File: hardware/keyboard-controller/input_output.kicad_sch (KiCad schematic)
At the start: 20 parts, among them J4 SYNC_IN, J5 CV_OUT, J6 GATE_OUT, J7 SYNC_OUT, Q1 2N3904, U9 LM358

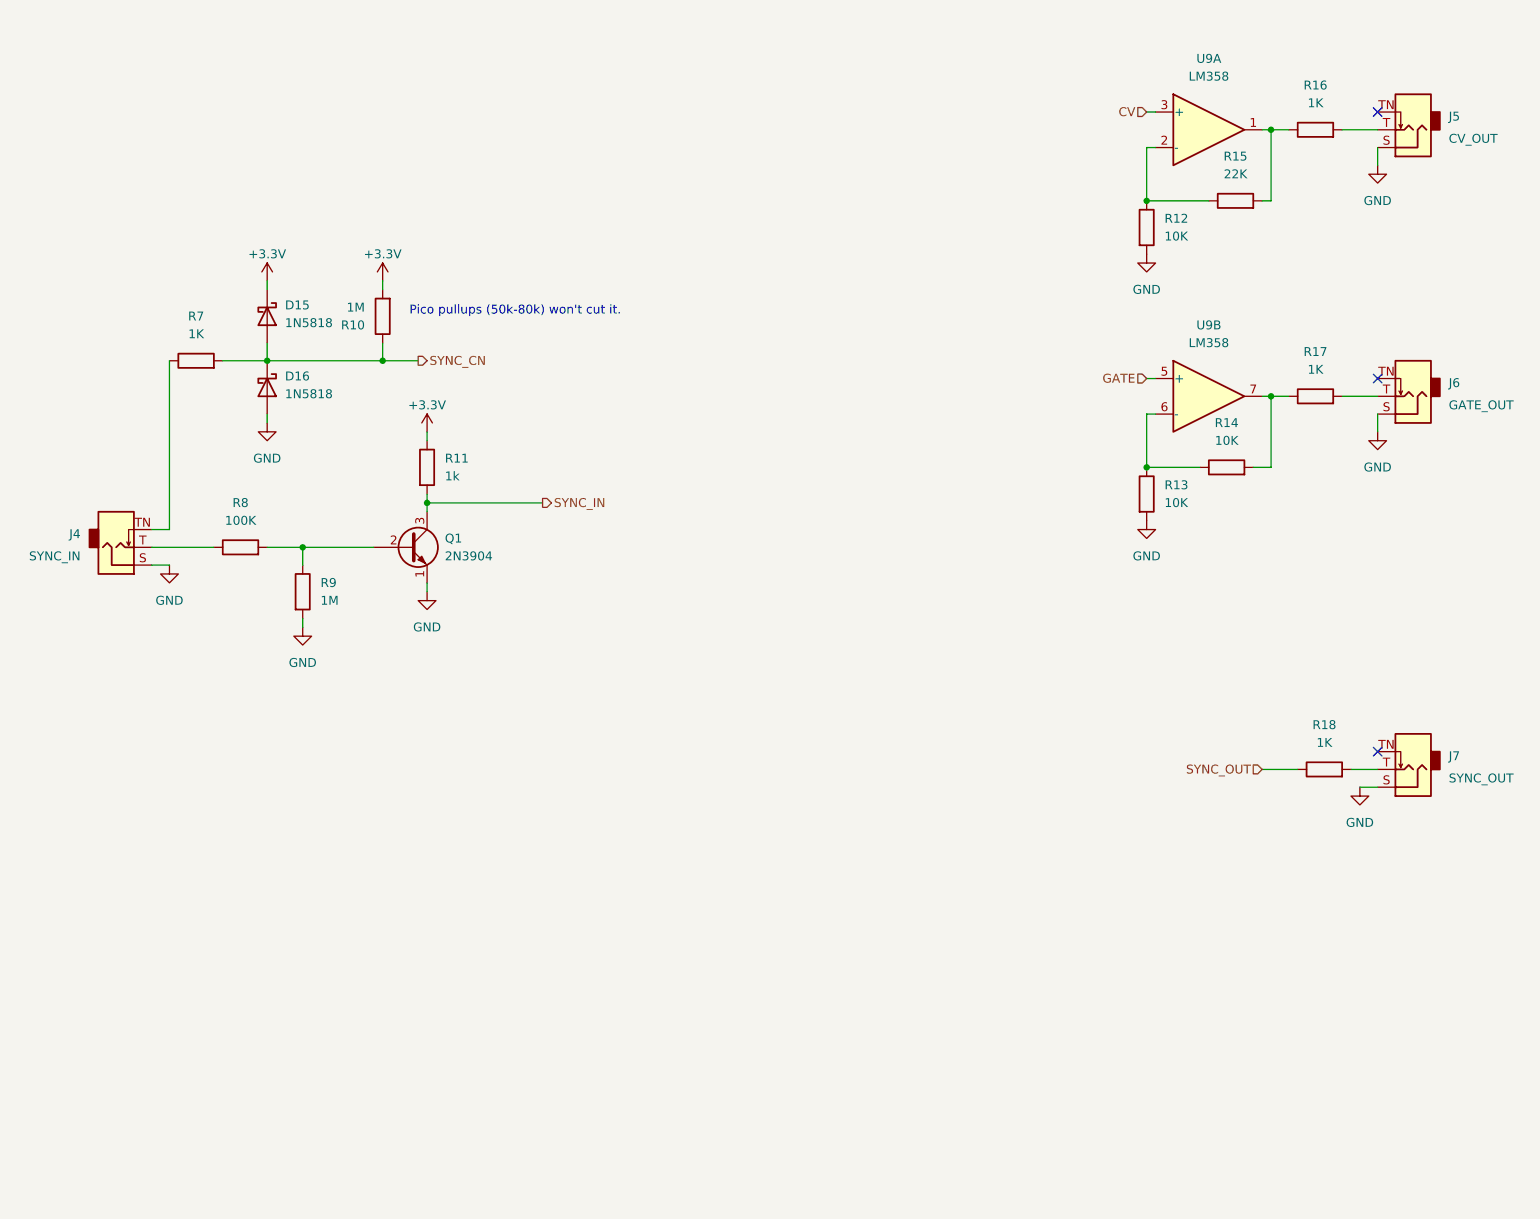
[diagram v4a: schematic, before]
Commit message: Completed schematic rev1. Started placing pcb
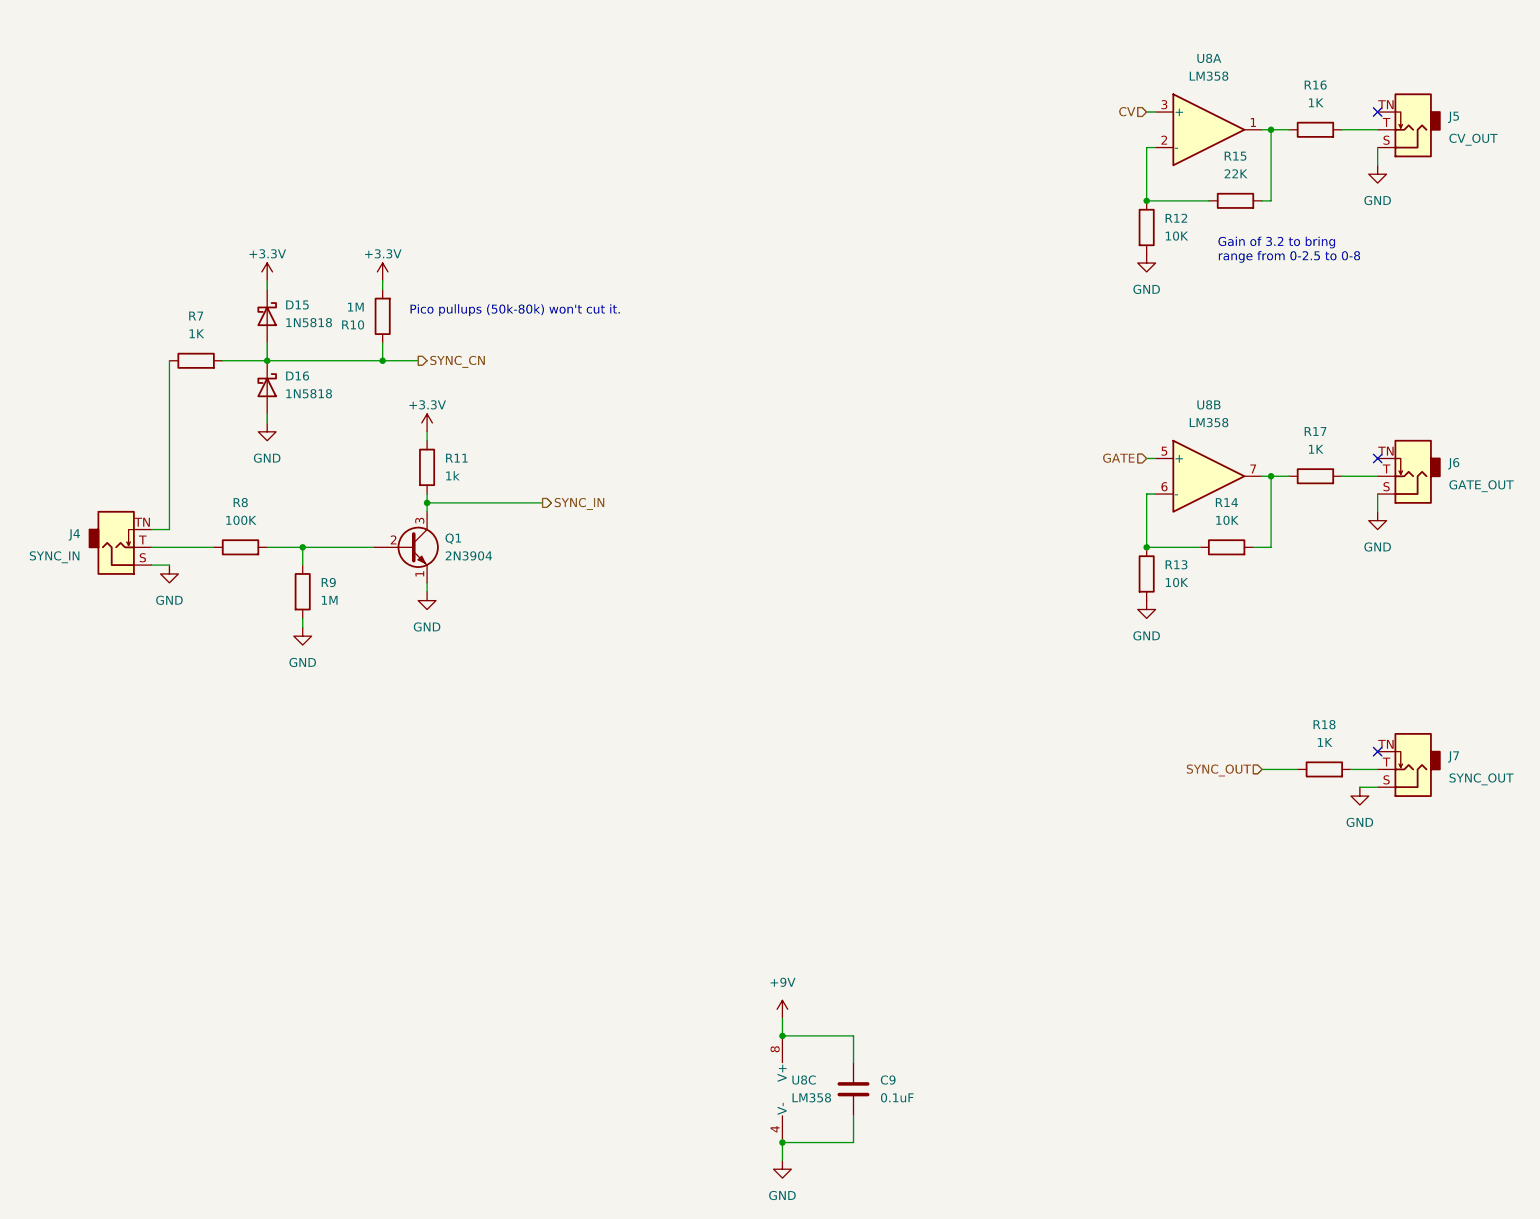
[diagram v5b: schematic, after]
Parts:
- added C9: 0.1uF, AEC_Capacitors:C_Disc_D5.0mm_W2.5mm_P3.0mm, symbol Device:C
- added unit 3 of U8
- R10, R11, R18, R7, R8, R9: footprint (none) -> Royal_Ohm_Resistors:R_Axial_DIN0207_L6.8mm_D2.5mm_P10.16mm_Horizontal
- renumbered U9 to U8
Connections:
- net GND: now also C9.2, U8.4 (V-)
- new net +9V: C9.1, U8.8 (V+)
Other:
- note added: "Gain of 3.2 to bring range from 0-2.5 to 0-8"
- moved on the sheet: J6, R13, R14, R17, U8B

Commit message: Completed initial pcb design
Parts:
- added C9: 0.1uF, AEC_Capacitors:C_Disc_D5.0mm_W2.5mm_P3.0mm, symbol Device:C
- added R14: 20K, Royal_Ohm_Resistors:R_Axial_DIN0207_L6.8mm_D2.5mm_P10.16mm_Horizontal, symbol Device:R
- added R17: 10K, Royal_Ohm_Resistors:R_Axial_DIN0207_L6.8mm_D2.5mm_P10.16mm_Horizontal, symbol Device:R
- added U8: LM358, Package_DIP:DIP-8_W7.62mm_Socket, symbol Amplifier_Operational:LM358
- R13: value 10K -> 20K
- renumbered C9 to C10, R14 to R15, R15 to R16, R16 to R18, R17 to R19, R18 to R20, U8 to U9
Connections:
- net +9V: now also C9.1, U8.8 (V+)
- net GND: now also C9.2, R14.2, U8.4 (V-), U8.5 (+)
- net SYNC_OUT: now also U8.3 (+); no longer R20.1
- net +3V3 renamed +3.3V
- new net: R14.1, R17.1, U8.2 (-)
- new net: U8.6 (-), U8.7
- new net: R17.2, R20.1, U8.1
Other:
- note added: "3.3v pulse -> 5v pulse"
- note added: "Unused"
- moved on the sheet: J5, J6, J7, R12, R13, R15, R16, R18, R19, R20, U9A, U9B

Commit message: Added more text detail to PCB. Completed more of BOM
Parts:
- D15, D16: Manufacturer (none) -> TEC; Manufacturer Part No. (none) -> 1N5818; Supplier Part No. (none) -> A-252
- J4, J5, J6, J7: Manufacturer (none) -> Tayda; Manufacturer Part No. (none) -> PJ-629HAN-05; Supplier Part No. (none) -> A-6040
- Q1: Manufacturer (none) -> Fairchild; Manufacturer Part No. (none) -> 2N3904; Supplier Part No. (none) -> A-111
- U8: Supplier (none) -> Tayda
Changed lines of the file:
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@@
+      (effects (font (size 1.27 1.27)) hide)
+    )
+    (property "Manufacturer" "Tayda" (id 5) (at 48.26 92.71 0)
+      (effects (font (size 1.27 1.27)) hide)
+    )
+    (property "Manufacturer Part No." "PJ-629HAN-05" (id 6) (at 48.26 92.71 0)
+      (effects (font (size 1.27 1.27)) hide)
+    )
+    (property "Supplier Part No." "A-6040" (id 7) (at 48.26 92.71 0)
       (effects (font (size 1.27 1.27)) hide)
     )
@@
     )
     (property "Supplier" "Tayda" (id 4) (at 69.85 69.85 0)
+      (effects (font (size 1.27 1.27)) hide)
+    )
+    (property "Manufacturer" "TEC" (id 5) (at 69.85 69.85 0)
+      (effects (font (size 1.27 1.27)) hide)
+    )
+    (property "Manufacturer Part No." "1N5818" (id 6) (at 69.85 69.85 0)
+      (effects (font (size 1.27 1.27)) hide)
+    )
+    (property "Supplier Part No." "A-252" (id 7) (at 69.85 69.85 0)
       (effects (font (size 1.27 1.27)) hide)
     )
@@
       (effects (font (size 1.27 1.27)) hide)
     )
+    (property "Manufacturer" "Tayda" (id 5) (at 233.68 69.85 0)
+      (effects (font (size 1.27 1.27)) hide)
+    )
+    (property "Manufacturer Part No." "PJ-629HAN-05" (id 6) (at 233.68 69.85 0)
+      (effects (font (size 1.27 1.27)) hide)
+    )
+    (property "Supplier Part No." "A-6040" (id 7) (at 233.68 69.85 0)
+      (effects (font (size 1.27 1.27)) hide)
+    )
     (pin "S")
     (pin "T")
@@
     )
     (property "Datasheet" "http://www.ti.com/lit/ds/symlink/lm2904-n.pdf" (id 3) (at 97.79 167.64 0)
+      (effects (font (size 1.27 1.27)) hide)
+    )
+    (property "Supplier" "Tayda" (id 4) (at 97.79 167.64 0)
       (effects (font (size 1.27 1.27)) hide)
     )
@@
       (effects (font (size 1.27 1.27)) hide)
     )
+    (property "Manufacturer" "Tayda" (id 5) (at 233.68 27.94 0)
+      (effects (font (size 1.27 1.27)) hide)
+    )
+    (property "Manufacturer Part No." "PJ-629HAN-05" (id 6) (at 233.68 27.94 0)
+      (effects (font (size 1.27 1.27)) hide)
+    )
+    (property "Supplier Part No." "A-6040" (id 7) (at 233.68 27.94 0)
+      (effects (font (size 1.27 1.27)) hide)
+    )
     (pin "S")
     (pin "T")
@@
     )
     (property "Supplier" "Tayda" (id 4) (at 69.85 59.69 0)
+      (effects (font (size 1.27 1.27)) hide)
+    )
+    (property "Manufacturer" "TEC" (id 5) (at 69.85 59.69 0)
+      (effects (font (size 1.27 1.27)) hide)
+    )
+    (property "Manufacturer Part No." "1N5818" (id 6) (at 69.85 59.69 0)
+      (effects (font (size 1.27 1.27)) hide)
+    )
+    (property "Supplier Part No." "A-252" (id 7) (at 69.85 59.69 0)
       (effects (font (size 1.27 1.27)) hide)
     )
@@
     )
     (property "Supplier" "Tayda" (id 4) (at 233.68 118.11 0)
+      (effects (font (size 1.27 1.27)) hide)
+    )
+    (property "Manufacturer" "Tayda" (id 5) (at 233.68 118.11 0)
+      (effects (font (size 1.27 1.27)) hide)
+    )
+    (property "Manufacturer Part No." "PJ-629HAN-05" (id 6) (at 233.68 118.11 0)
+      (effects (font (size 1.27 1.27)) hide)
+    )
+    (property "Supplier Part No." "A-6040" (id 7) (at 233.68 118.11 0)
       (effects (font (size 1.27 1.27)) hide)
     )
@@
       (effects (font (size 1.27 1.27)) hide)
     )
+    (property "Manufacturer" "Fairchild" (id 5) (at 90.17 92.71 0)
+      (effects (font (size 1.27 1.27)) hide)
+    )
+    (property "Manufacturer Part No." "2N3904" (id 6) (at 90.17 92.71 0)
+      (effects (font (size 1.27 1.27)) hide)
+    )
+    (property "Supplier Part No." "A-111" (id 7) (at 90.17 92.71 0)
+      (effects (font (size 1.27 1.27)) hide)
+    )
     (pin "1")
     (pin "2")
@@
     )
     (property "Datasheet" "http://www.ti.com/lit/ds/symlink/lm2904-n.pdf" (id 3) (at 135.89 170.18 0)
+      (effects (font (size 1.27 1.27)) hide)
+    )
+    (property "Supplier" "Tayda" (id 4) (at 135.89 170.18 0)
       (effects (font (size 1.27 1.27)) hide)
     )
@@
       (effects (font (size 1.27 1.27)) hide)
     )
+    (property "Supplier" "Tayda" (id 4) (at 205.74 118.11 0)
+      (effects (font (size 1.27 1.27)) hide)
+    )
